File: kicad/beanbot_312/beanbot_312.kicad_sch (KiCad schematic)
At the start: 66 parts, among them M1 P&O2_VOEDING, M10 P&O2_MEETPUNT, M11 P&O2_ULTRASONE_HC_SR04, M12 P&O2_MEETPUNT, M13 P&O2_MEETPUNT, M14 P&O2_GEWICHTSENSOR, M15 P&O2_MEETPUNT, M16 P&O2_MEETPUNT, M17 P&O2_MEETPUNT, M18 P&O2_MEETPUNT, M19 P&O2_MEETPUNT, M2 P&O2_MEETPUNT, M20 P&O2_KLEURSENSOR, M21 P&O2_MEETPUNT, M22 P&O2_MEETPUNT, M23 P&O2_RESISTOR, M24 P&O2_MEETPUNT, M25 P&O2_RESISTOR, M26 P&O2_RESISTOR, M27 P&O2_MEETPUNT, M28 P&O2_DC-MOTOR, M29 P&O2_RESISTOR, M3 P&O2_RESISTOR, M30 P&O2_MEETPUNT, M31 P&O2_DC-MOTOR, M32 P&O2_MEETPUNT, M33 P&O2_RESISTOR, M34 P&O2_MEETPUNT, M35 P&O2_RESISTOR, M36 P&O2_RESISTOR, M37 P&O2_MEETPUNT, M38 P&O2_DC-MOTOR, M39 P&O2_RESISTOR, M4 P&O2_MEETPUNT, M40 P&O2_MEETPUNT, M41 P&O2_DC-MOTOR, M42 P&O2_MEETPUNT, M43 P&O2_RESISTOR, M44 P&O2_MEETPUNT, M45 P&O2_RESISTOR, M46 P&O2_RESISTOR, M47 P&O2_MEETPUNT, M48 P&O2_DC-MOTOR, M49 P&O2_RESISTOR, M5 P&O2_RGB_LED, M50 P&O2_MEETPUNT, M51 P&O2_DC-MOTOR, M52 P&O2_MEETPUNT, M6 P&O2_RESISTOR, M7 P&O2_MEETPUNT, M8 P&O2_RESISTOR, M9 P&O2_RESISTOR, U1 P&O2_ARDUINO_MEGA, U2 LCD-016N002L

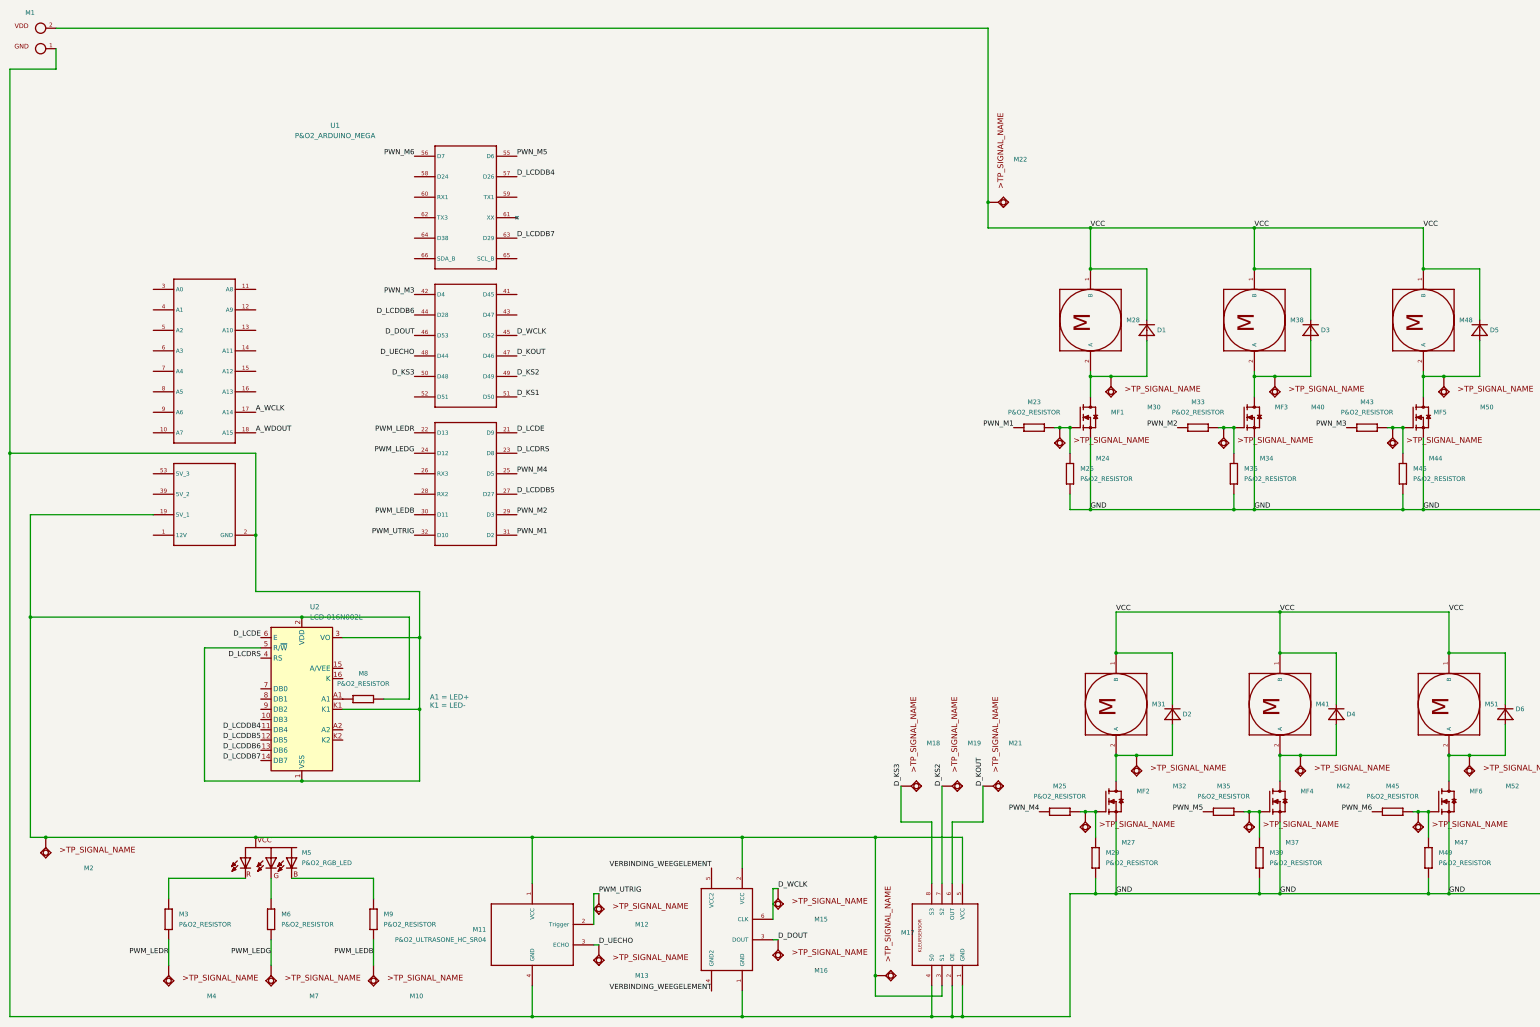
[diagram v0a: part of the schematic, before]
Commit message: Added labels and modified LCD
I added some labels and renamed some others and I placed the LCD vertically instead of horizontally, like asked in the assignment. Please review my changes so that I didn't made some stupid mistake.
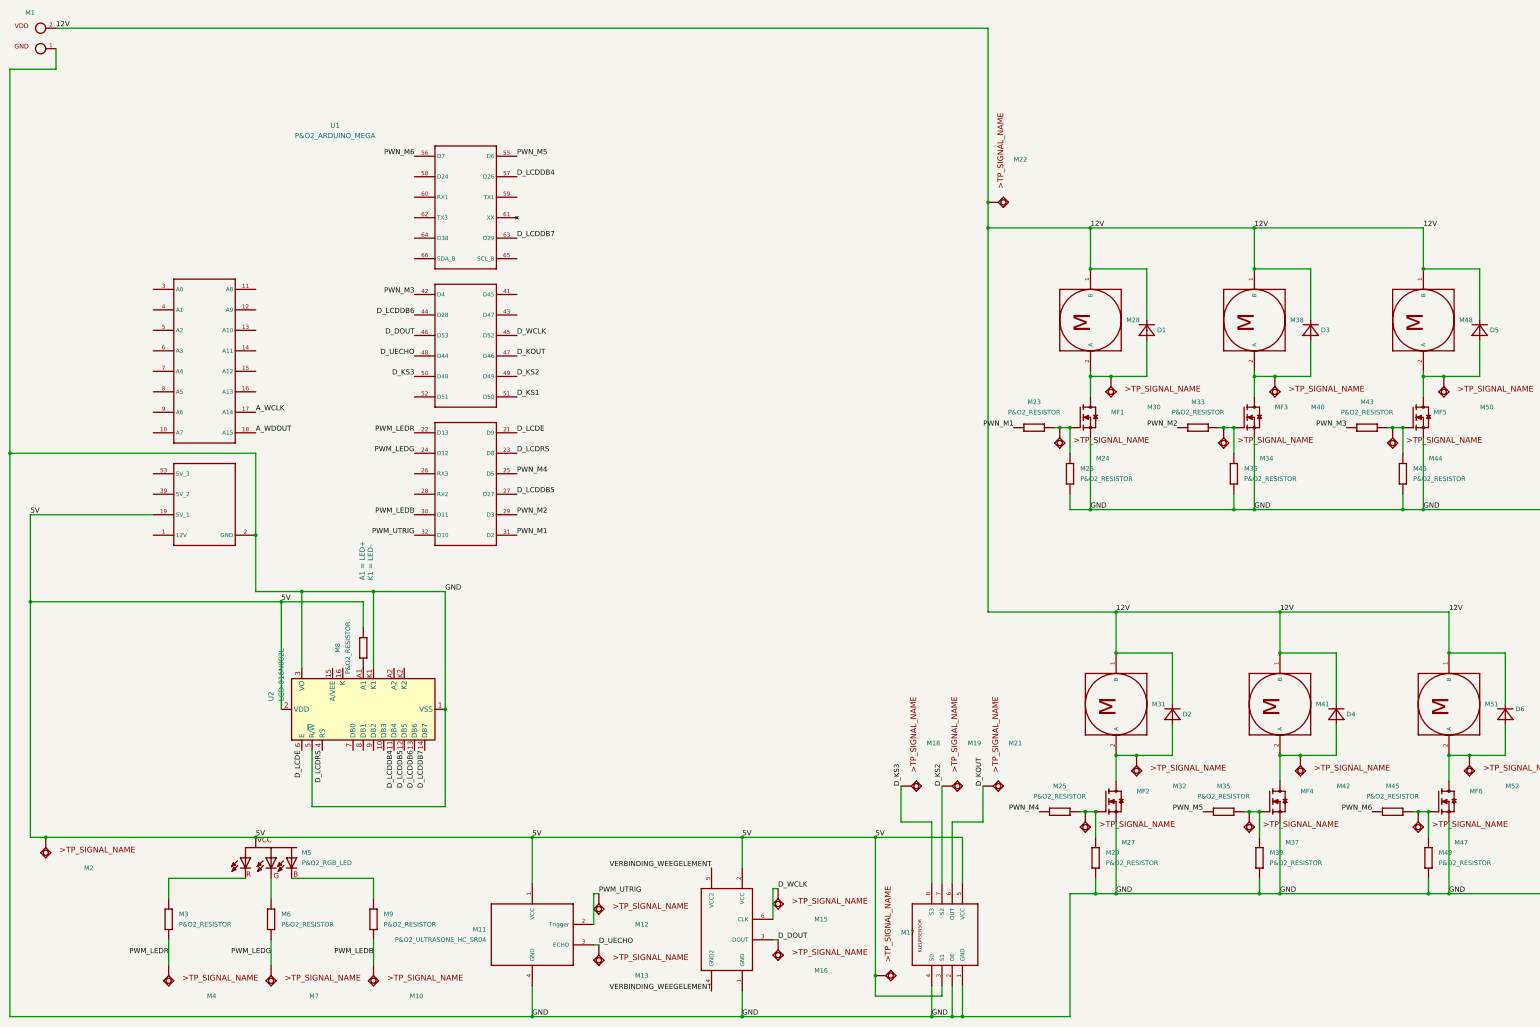
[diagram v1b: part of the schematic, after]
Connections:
- net 5V: now reaches M11.1 (VCC), M14.2 (VCC), M17.1 (TP), M2.1 (TP), M20.3 (S1), M20.5 (VCC), M5.2 (VCC), M8.2, U1.19 (5V_1), U2.2 (VDD)
- net VCC renamed 12V
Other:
- moved on the sheet: M8, U2

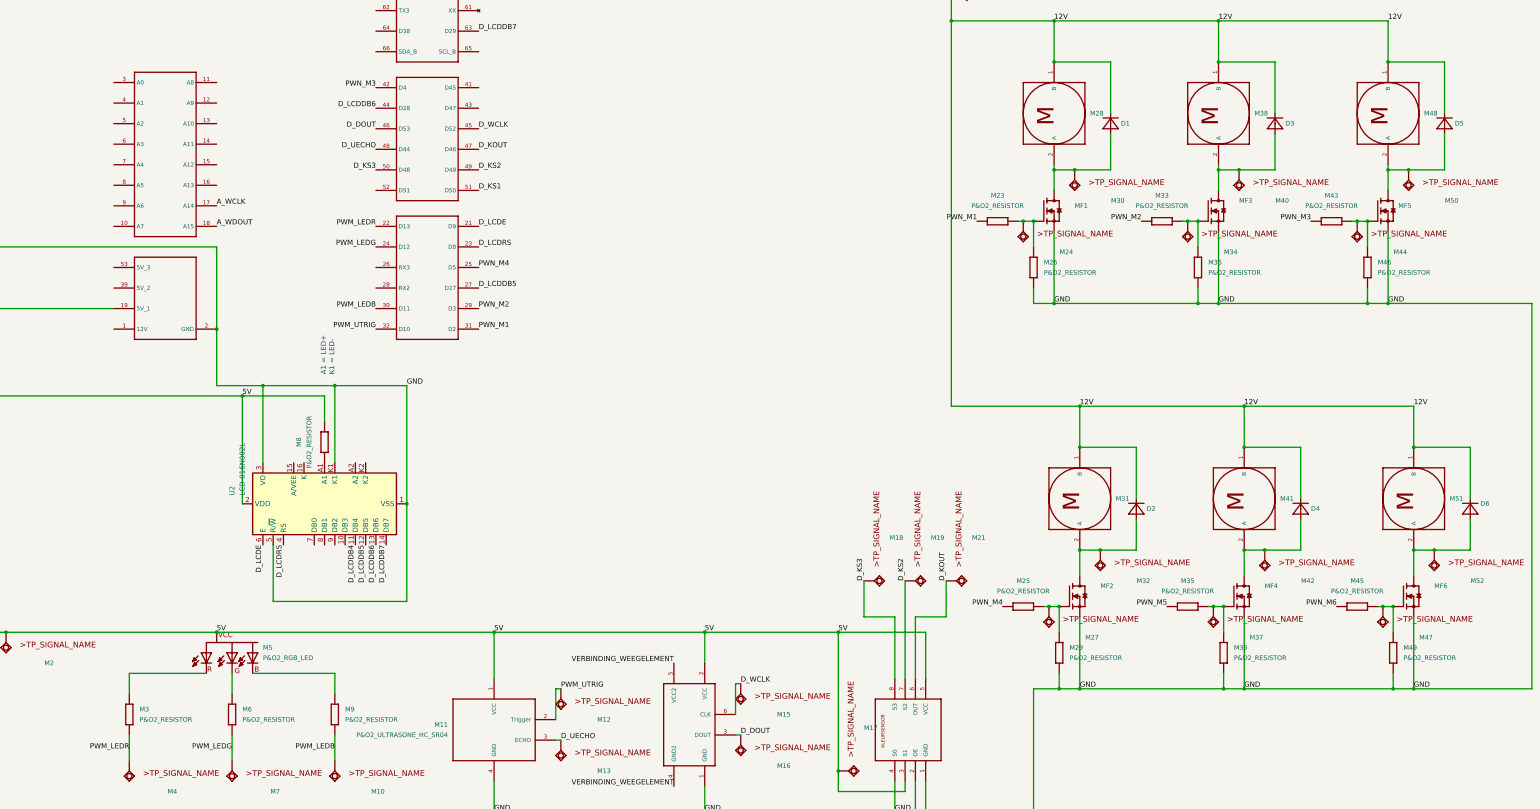
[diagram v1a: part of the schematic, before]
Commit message: Updated footprints and balance
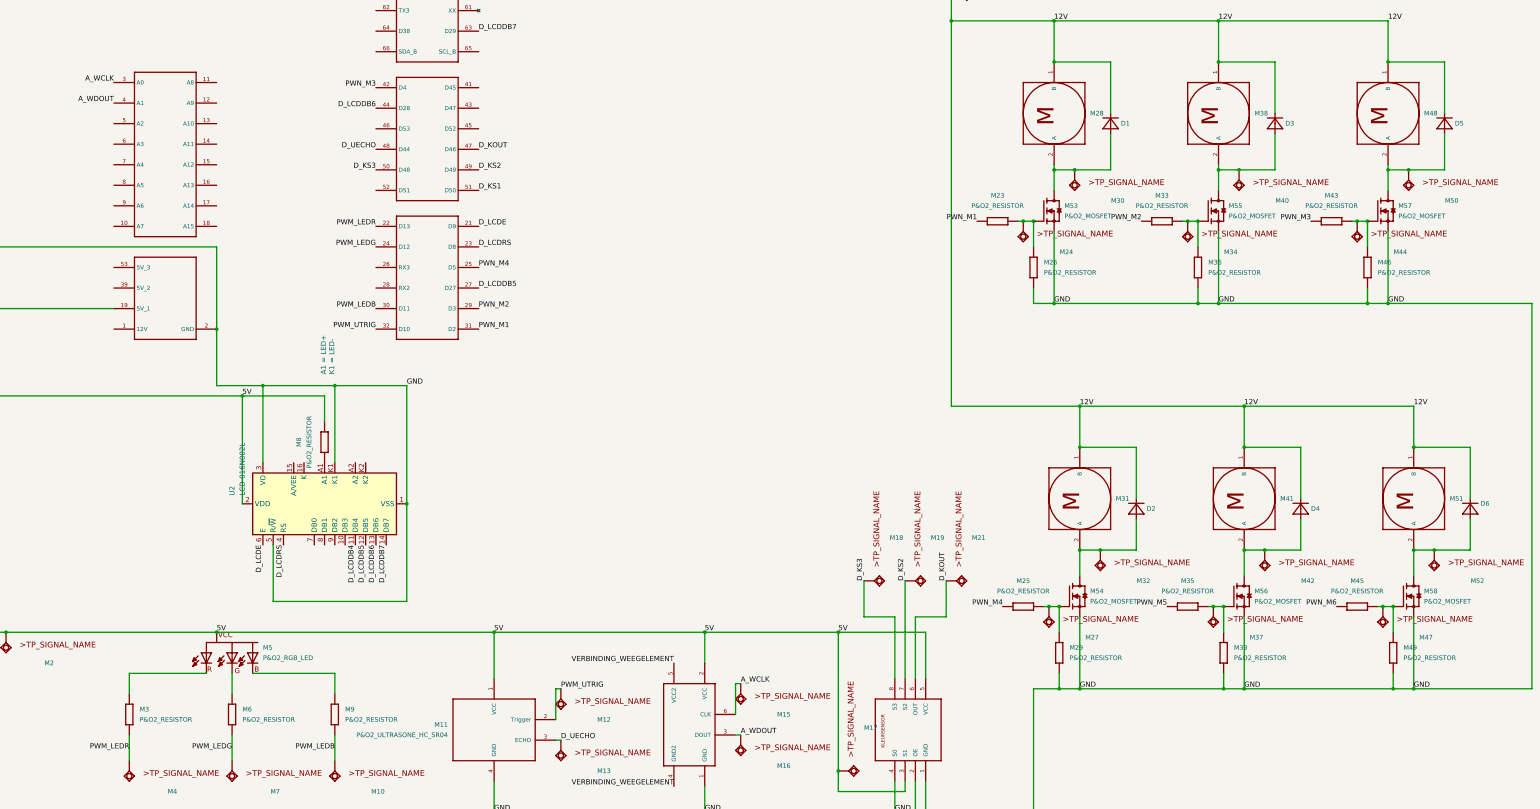
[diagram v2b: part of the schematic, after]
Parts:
- removed MF1, MF2, MF3, MF4, MF5: P&O2_MOSFET, P&O2_lib_TO220V, symbol 1_P&O2_lib:P&O2_MOSFET
- removed MF6: \, P&O2_lib_TO220V, symbol 1_P&O2_lib:P&O2_MOSFET
- added M53, M54, M55, M56, M57, M58: P&O2_MOSFET, 1_P&O2_lib:P&O2_TO220, symbol 1_P&O2_lib:P&O2_MOSFET
- D1, D2, D3, D4, D5, D6: footprint P&O2_lib_D-12.5 -> 1_P&O2_lib:P&O2_DIODE
- M1, M28, M31, M38, M41, M48, M51: footprint P&O2_lib_MKDSN1_5_2-5_08 -> 1_P&O2_lib:P&O2_2PIN-SCREW-5.08
- M10, M12, M13, M15, M16, M17, M18, M19, M2, M21, M22, M24, M27, M30, M32, M34, M37, M4, M40, M42, M44, M47, M50, M52, M7: footprint P&O2_lib_MEETPUNT -> 1_P&O2_lib:P&O2_MEETPUNT
- M11: footprint P&O2_lib_MA04-1 -> 1_P&O2_lib:P&O2_ULTRASONE
- M14: footprint P&O2_lib_GEWICHTSENSOR-6PIN -> 1_P&O2_lib:P&O2_GEWICHTSENSOR-6PIN
- M20: footprint P&O2_lib_KLRS_FP -> 1_P&O2_lib:P&O2_KLEURENSENSOR-8PIN
- M23, M25, M26, M29, M3, M33, M35, M36, M39, M43, M45, M46, M49, M6, M8, M9: footprint P&O2_lib_0411_15 -> 1_P&O2_lib:P&O2_RES
- M5: footprint P&O2_lib_2PIN-HEADER-LED -> 1_P&O2_lib:P&O2_RGB_LED
- U1: footprint (none) -> 1_P&O2_lib:P&O2_ARDUINO_MEGA
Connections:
- net A_WCLK: now also M14.6 (CLK), M15.1 (TP), U1.3 (A0); no longer U1.17 (A14)
- net A_WDOUT: now also M14.3 (DOUT), M16.1 (TP), U1.4 (A1); no longer U1.18 (A15)
- net GND: now also M53.3 (S), M54.3 (S), M55.3 (S), M56.3 (S), M57.3 (S), M58.3 (S)
- net at M25.2, M27.1 (TP), M29.1: now also M54.1 (eG)
- net at D2.A, M31.2 (A), M32.1 (TP): now also M54.2 (D)
- net at M35.2, M37.1 (TP), M39.1: now also M56.1 (eG)
- net at M33.2, M34.1 (TP), M36.1: now also M55.1 (eG)
- net at M45.2, M47.1 (TP), M49.1: now also M58.1 (eG)
- net at D1.A, M28.2 (A), M30.1 (TP): now also M53.2 (D)
- net at D6.A, M51.2 (A), M52.1 (TP): now also M58.2 (D)
- net at M43.2, M44.1 (TP), M46.1: now also M57.1 (eG)
- net at D4.A, M41.2 (A), M42.1 (TP): now also M56.2 (D)
- net at M23.2, M24.1 (TP), M26.1: now also M53.1 (eG)
- net at D5.A, M48.2 (A), M50.1 (TP): now also M57.2 (D)
- net at D3.A, M38.2 (A), M40.1 (TP): now also M55.2 (D)
- removed net D_DOUT: M14.3 (DOUT), M16.1 (TP), U1.46 (D53)
- removed net D_WCLK: M14.6 (CLK), M15.1 (TP), U1.45 (D52)
